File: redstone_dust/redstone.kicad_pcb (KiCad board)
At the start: 2 copper layers, 40 x 40 mm, 76 parts, among them J1 1x4_Pogo, J2 1x4_Pogo, J3 1x4_Pogo, J4 1x4_Pogo, J5 1x4_Pogo, J6 1x4_Pogo, J7 1x4_Pogo, J8 1x4_Pogo, Q1 BC108, Q2 BC108, Q3 BC108, Q4 BC108, SW1 SW_Push_Open, U1 RP2040, U2 RBT05W24S05, U3 TPS62162DSG, U5 W25Q16JVSS

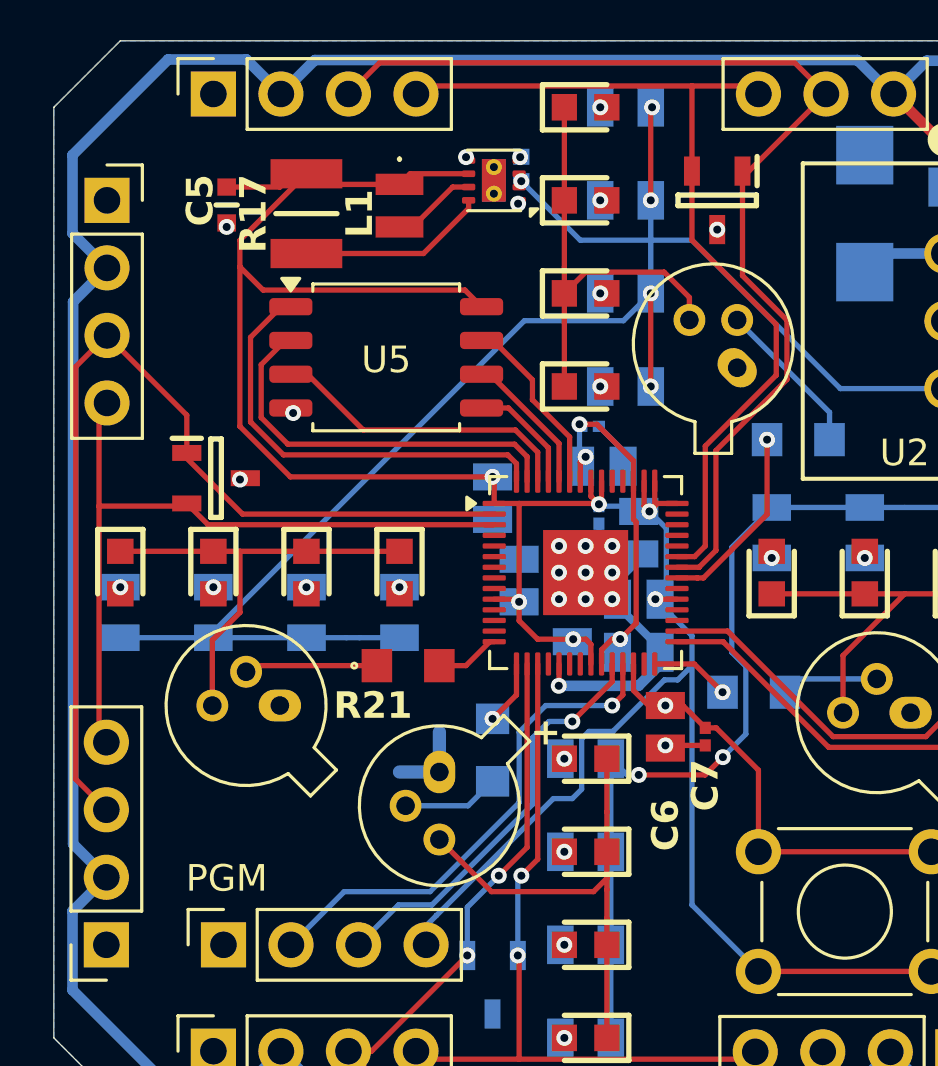
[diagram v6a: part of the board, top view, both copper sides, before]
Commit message: fix all silkscreen drc errors
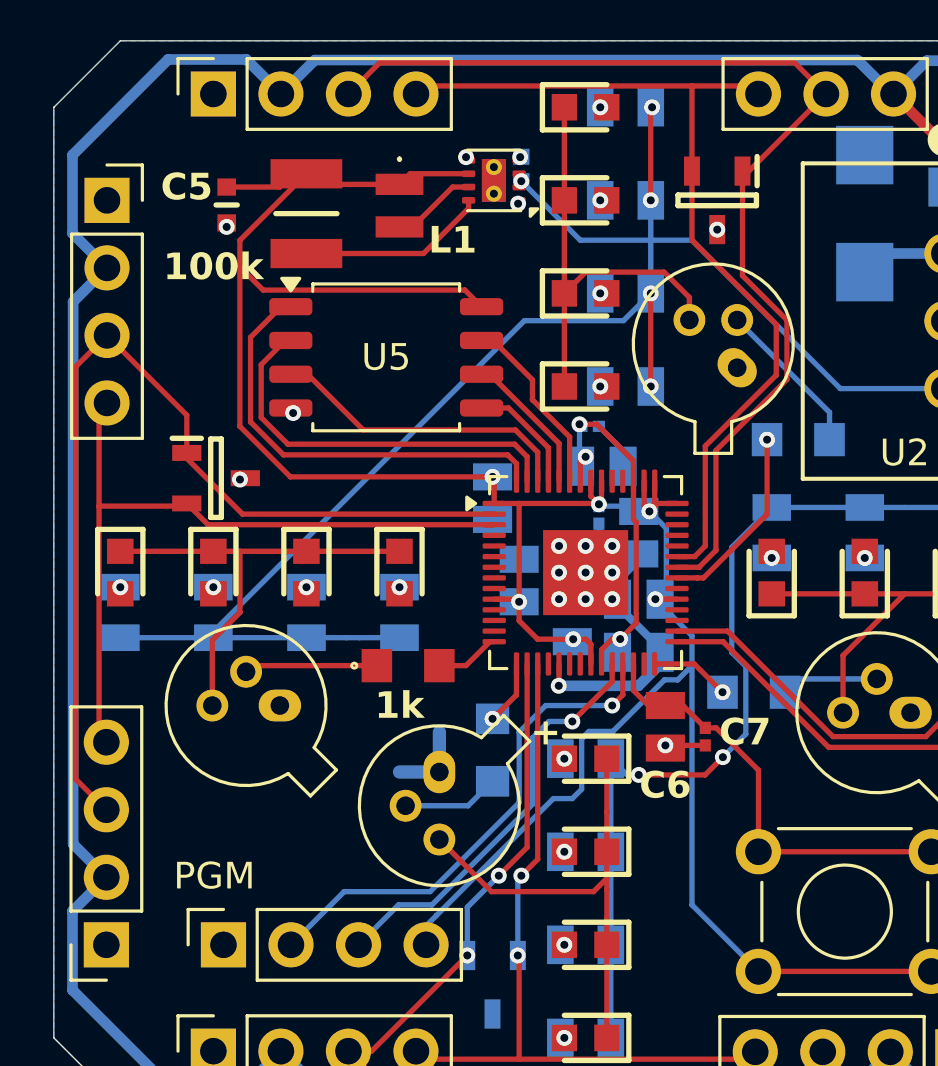
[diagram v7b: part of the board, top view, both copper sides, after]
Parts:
- renumbered R17 to 100k, R21 to 1k, R18 to 1k, R19 to 1k, R20 to 1k, R15 to 200, R11 to 200, R6 to 200, R1 to 200, PGM to J9
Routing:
- net Net-(SW1-B): vias 1 -> 0
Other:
- board text added: "PGM"
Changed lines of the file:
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@@
 		(descr "Through hole straight socket strip, 1x04, 2.54mm pitch, single row (from Kicad 4.0.7), script generated")
 		(tags "Through hole socket strip THT 1x04 2.54mm single row")
-		(property "Reference" "PGM"
+		(property "Reference" "J9"
 			(at 2.5 0.12 180)
 			(layer "F.SilkS")
+			(hide yes)
 			(effects
 				(font
@@
 		(tags "Capacitor")
 		(property "Reference" "C7"
-			(at 1.83 0 90)
+			(at -0.17 -1.5 180)
 			(layer "F.SilkS")
 			(effects
@@
 		(tags "Inductor")
 		(property "Reference" "L1"
-			(at 0.3 1.5 90)
+			(at 1.3 -2 180)
 			(layer "F.SilkS")
 			(effects
@@
 		(descr "ERJUP6")
 		(tags "Resistor")
-		(property "Reference" "R21"
-			(at -1.325 1.5 0)
+		(property "Reference" "1k"
+			(at -0.325 1.5 0)
 			(layer "F.SilkS")
 			(effects
@@
 		(tags "Capacitor")
 		(property "Reference" "C5"
-			(at -0.175 1 270)
+			(at -0.675 1.5 0)
 			(layer "F.SilkS")
 			(effects
@@
 		(descr "1210 (3225 Metric)")
 		(tags "Resistor")
-		(property "Reference" "R17"
-			(at 0 2 90)
+		(property "Reference" "100k"
+			(at 2 3.5 180)
 			(layer "F.SilkS")
 			(effects
@@
 		(tags "SOIC SO P-SOP SOP SOP-8 SO SO-8 8S2 S2AE/F K04-056 CASE-751BE SO8W 8-Pin-SOIC PSA W8-2 W8-4 W8MS-1 FPT-8P-M08")
 		(property "Reference" "U5"
-			(at 0 0.095 0)
+			(at 0 0 0)
 			(layer "F.SilkS")
 			(effects
@@
 		(tags "Capacitor")
 		(property "Reference" "C6"
-			(at 3.7 0 270)
+			(at 2.2 0 0)
 			(layer "F.SilkS")
 			(effects
@@
 		(descr "TNPW0805 e3")
 		(tags "Resistor")
-		(property "Reference" "R15"
+		(property "Reference" "200"
 			(at 0 -1.5 90)
 			(layer "B.SilkS")
@@
 		(descr "TNPW0805 e3")
 		(tags "Resistor")
-		(property "Reference" "R11"
+		(property "Reference" "200"
 			(at 0 -2 0)
 			(layer "B.SilkS")
@@
 		(tags "Capacitor")
 		(property "Reference" "C2"
-			(at 0 0 90)
+			(at 0 1.5 90)
 			(layer "B.SilkS")
 			(effects
 				(font
-					(size 1.27 1.27)
-					(thickness 0.254)
+					(size 1 1)
+					(thickness 0.15)
 				)
 				(justify mirror)
@@
 		(tags "Capacitor")
 		(property "Reference" "C2"
-			(at 0 0 90)
+			(at 0 -1.5 90)
 			(layer "B.SilkS")
 			(effects
 				(font
-					(size 1.27 1.27)
-					(thickness 0.254)
+					(size 1 1)
+					(thickness 0.15)
 				)
 				(justify mirror)
@@
 		(tags "Capacitor")
 		(property "Reference" "C1"
-			(at -0.18 1.42 270)
+			(at 1.82 -0.08 270)
 			(layer "B.SilkS")
 			(effects
@@
 		(tags "Capacitor")
 		(property "Reference" "C2"
-			(at -0.2 0 90)
+			(at -0.7 -2 180)
 			(layer "B.SilkS")
 			(effects
@@
 		(tags "Capacitor")
 		(property "Reference" "C9"
-			(at 0 0 0)
+			(at -1.67 0 0)
 			(layer "B.SilkS")
 			(effects
 				(font
-					(size 1.27 1.27)
-					(thickness 0.254)
+					(size 1 1)
+					(thickness 0.15)
 				)
 				(justify mirror)
@@
 		(descr "TNPW0805 e3")
 		(tags "Resistor")
-		(property "Reference" "R6"
+		(property "Reference" "200"
 			(at 0 1.5 90)
 			(layer "B.SilkS")
@@
 		(descr "TNPW0805 e3")
 		(tags "Resistor")
-		(property "Reference" "R1"
+		(property "Reference" "200"
 			(at 0 -5.5 0)
 			(layer "B.SilkS")
@@
 		(tags "Capacitor")
 		(property "Reference" "C3"
-			(at 2.3 -1.5 0)
+			(at 1.3 -1.5 0)
 			(layer "B.SilkS")
 			(effects
@@
 		(tags "Capacitor")
 		(property "Reference" "C2"
-			(at 0 0 90)
+			(at 0 -1.5 90)
 			(layer "B.SilkS")
 			(effects
 				(font
-					(size 1.27 1.27)
-					(thickness 0.254)
+					(size 1 1)
+					(thickness 0.15)
 				)
 				(justify mirror)
@@
 		(tags "Capacitor")
 		(property "Reference" "C10"
-			(at 0 0 0)
+			(at 2.89 0 0)
 			(layer "B.SilkS")
 			(effects
 				(font
-					(size 1.27 1.27)
-					(thickness 0.254)
+					(size 1 1)
+					(thickness 0.15)
 				)
 				(justify mirror)
@@
 		(descr "ERJUP6")
 		(tags "Resistor")
-		(property "Reference" "R18"
-			(at -3 0 180)
+		(property "Reference" "1k"
+			(at 0 1.5 180)
 			(layer "B.SilkS")
 			(effects
@@
 		(descr "ERJUP6")
 		(tags "Resistor")
-		(property "Reference" "R19"
-			(at -1.175 1.5 180)
+		(property "Reference" "1k"
+			(at -0.175 -1.5 180)
 			(layer "B.SilkS")
 			(effects
@@
 		(tags "Capacitor")
 		(property "Reference" "C10"
-			(at 0 0 0)
+			(at 3 0 0)
 			(layer "B.SilkS")
 			(effects
 				(font
-					(size 1.27 1.27)
-					(thickness 0.254)
+					(size 1 1)
+					(thickness 0.15)
 				)
 				(justify mirror)
@@
 		(tags "Capacitor")
 		(property "Reference" "C2"
-			(at 0 0 0)
+			(at -2.5 0 0)
 			(layer "B.SilkS")
 			(effects
 				(font
-					(size 1.27 1.27)
-					(thickness 0.254)
+					(size 1 1)
+					(thickness 0.15)
 				)
 				(justify mirror)
@@
 		(descr "ERJUP6")
 		(tags "Resistor")
-		(property "Reference" "R20"
-			(at 2.675 0 90)
+		(property "Reference" "1k"
+			(at 1.675 -1.5 90)
 			(layer "B.SilkS")
 			(effects
@@
 		(tags "Capacitor")
 		(property "Reference" "C4"
-			(at 3 0 270)
+			(at 2 0 0)
 			(layer "B.SilkS")
 			(effects
@@
 		(tags "Capacitor")
 		(property "Reference" "C11"
-			(at 0 0 90)
+			(at -0.83 2 90)
 			(layer "B.SilkS")
 			(effects
 				(font
-					(size 1.27 1.27)
-					(thickness 0.254)
+					(size 1 1)
+					(thickness 0.15)
 				)
 				(justify mirror)
@@
 		)
 	)
+	(gr_text "PGM"
+		(at 119.5 67 0)
+		(layer "F.SilkS")
+		(effects
+			(font
+				(size 1 1)
+				(thickness 0.15)
+			)
+			(justify left bottom)
+		)
+	)
 	(segment
 		(start 132.5 40)
@@
 		(net 72)
 	)
-	(via
-		(at 138 60)
-		(size 0.6)
-		(drill 0.3)
-		(layers "F.Cu" "B.Cu")
-		(net 72)
-	)

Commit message: finalize redstone dust
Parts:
- renumbered U2 to 5v, U5 to MEM
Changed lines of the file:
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@@
 		(at 148.5 43 -90)
 		(tags "RBT05W24S05 ")
-		(property "Reference" "U2"
+		(property "Reference" "5v"
 			(at 7.5 1.5 0)
 			(unlocked yes)
@@
 		(descr "SOIC, 8 Pin (JEITA/EIAJ ED-7311-19 variation 08-001-BBA and Atmel/Microchip, 208 mils width, https://www.jeita.or.jp/japanese/standard/book/ED-7311-19/#target/page_no=21, https://ww1.microchip.com/downloads/en/DeviceDoc/20005045C.pdf#page=23, https://ww1.microchip.com/downloads/en/DeviceDoc/doc2535.pdf#page=162), generated with kicad-footprint-generator ipc_gullwing_generator.py")
 		(tags "SOIC SO P-SOP SOP SOP-8 SO SO-8 8S2 S2AE/F K04-056 CASE-751BE SO8W 8-Pin-SOIC PSA W8-2 W8-4 W8MS-1 FPT-8P-M08")
-		(property "Reference" "U5"
+		(property "Reference" "MEM"
 			(at 0 0 0)
 			(layer "F.SilkS")
